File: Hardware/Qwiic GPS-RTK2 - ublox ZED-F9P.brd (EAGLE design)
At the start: 43.2 x 43.2 mm, 136 parts, among them J1 Radio, J13 U.FL, J3 PTH, U2 3.3V, U3 ZED-F9P

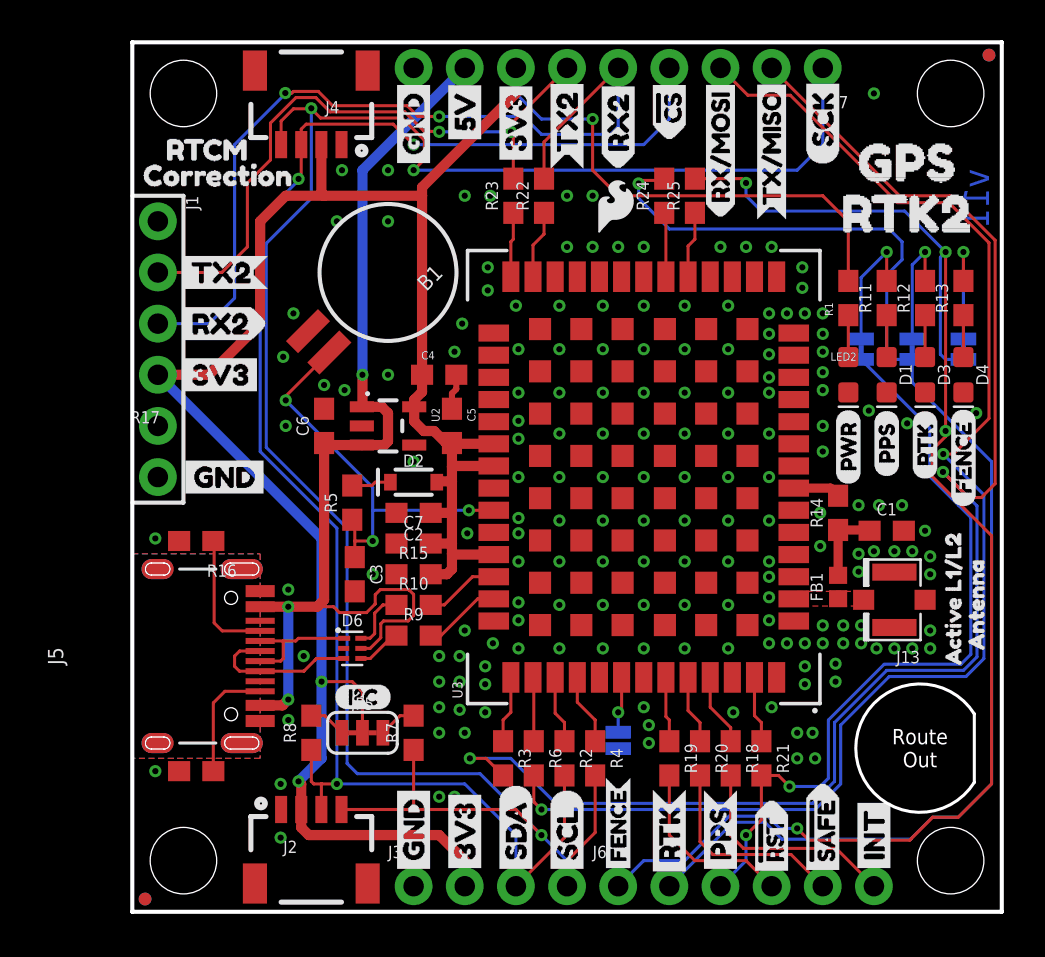
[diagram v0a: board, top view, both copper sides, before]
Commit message: Adding SMA connector to Antenna and SMA
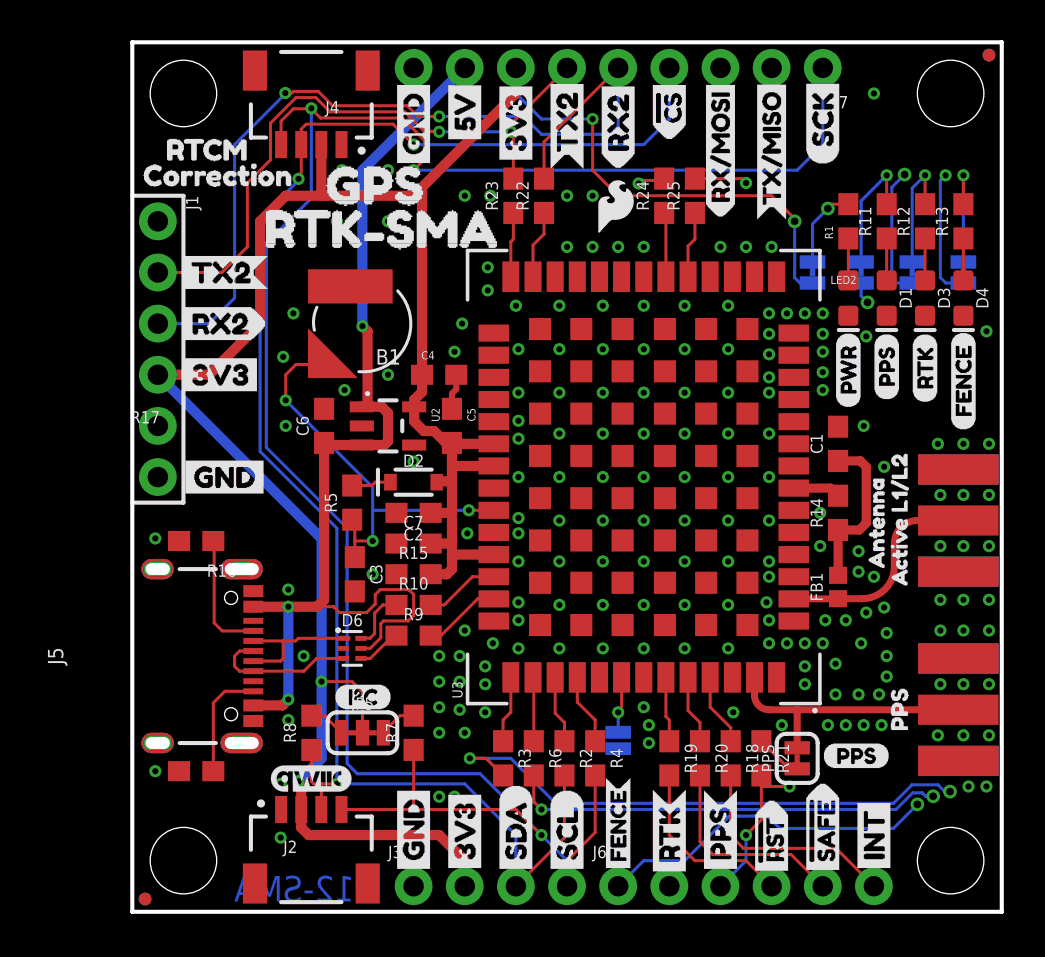
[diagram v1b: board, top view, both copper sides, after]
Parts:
- removed J13: U.FL, SparkFun-Connectors:U.FL
- removed JP1, JP2, JP3: (no value), SparkFun-Jumpers:SMT-JUMPER_2_NC_TRACE_SILK
- removed U$46: (no value), buzzard_labels (4):GPS#RTK28
- removed U$64: (no value), buzzard_labels (4):RTK21
- added E1, E2: SMA, SparkFun-RF:SMA-EDGE
- added FENCE, PPS, PPS_LED, PWR, RTK: (no value), SparkFun-Jumpers:SMT-JUMPER_2_NC_TRACE_SILK
- added U$47, U$74: (no value), buzzard_labels (2):PPS1
- added U$72: (no value), buzzard_labels (33):PPS0
- added U$73: (no value), buzzard_labels (3):RTK#SMA4
- added U$75: (no value), buzzard_labels (8):ANTENNA2
- added U$76: (no value), buzzard_labels (4):GPS#RTK#SMA5
- B1: device SparkFun-Batteries:BATTCON-6.8MM -> SparkFun-Batteries:ML414H_IV01E
- FB1: value FERRITE_BEAD-120_OHM-0402 -> 120_OHM
- J2, J4: value (none) -> Qwiic Right Angle; device SparkFun-Connectors:1X04_1MM_RA -> SparkFun-Connectors:JST04_1MM_RA
- J5: device SparkFun-Connectors:USB-C-16P -> SparkFun-Connectors:USB-C-16P-2LAYER-PADS
- U$12: device buzzard_labels:JP20 -> Labels:PWR-()-03
- U$25: device buzzard_labels (5):JP10 -> buzzard_labels (33):PPS0
- U$30: device Labels:QWIIC-LOGO-MEDIUM -> SparkFun-Aesthetics:QWIIC_4MM
- U$32: device buzzard_labels (5):JP32 -> buzzard_labels:RTK1
- U$54: value SMA-ANTENNA-THREADED -> (none); device SparkFun-Hardware:SMA-THREADED -> buzzard_labels:FENCE2
- moved U$59 26.4 mm to (8.00, 36.1)
- moved U$54 25.1 mm to (41.3, 33.1), flipped to the bottom, turned to 90 degrees
- moved U$71 6.41 mm to (37.0, 16.4)
- moved U$12 6.17 mm to (33.8, 33.1)
- moved C1 4.95 mm to (35.1, 23.2), turned to 90 degrees
- moved U$65 4.76 mm to (38.1, 15.5)
- moved U$32 4.47 mm to (38.7, 33.1)
- moved U$11 3.81 mm to (41.3, 23.9)
- moved D1 3.81 mm to (37.5, 30.5)
- moved D3 3.81 mm to (39.4, 30.5)
- moved D4 3.81 mm to (41.3, 30.5)
- moved LED2 3.81 mm to (35.6, 30.5)
- moved R1 3.81 mm to (35.6, 34.3)
- moved R11 3.81 mm to (37.5, 34.3)
- moved R12 3.81 mm to (39.4, 34.3)
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- renumbered JP4 to SPI
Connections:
- removed net SHLD: J5.SHLD1, J5.SHLD2, J5.SHLD3, J5.SHLD4, J5.SHLD5, J5.SHLD6, J5.SHLD7, J5.SHLD8
- new net N$21: PPS.1, R21.1
- new net PPS_STAT: J6.3, PPS_LED.2, R21.2
- net 3.3V: now also PWR.2; no longer R1.2
- net FENCE_STAT: now also FENCE.2; no longer JP3.2
- net GND: now also E1.GND@0, E1.GND@1, E1.GND@2, E1.GND@3, E2.GND@0, E2.GND@1, E2.GND@2, E2.GND@3, J5.SHLD1, J5.SHLD2, J5.SHLD3, J5.SHLD4; no longer J13.1, J13.2
- net GPS_ANT1: now also E1.SIG; no longer J13.FEED
- net N$17: now also PWR.1, R1.2; no longer R21.1, U3.53
- net N$3: now also RTK.1; no longer JP2.1
- net N$4: now also PPS_LED.1; no longer JP1.1
- net N$9: now also FENCE.1; no longer JP3.1
- net PPS: now also E2.SIG, PPS.2, U3.53; no longer J6.3, JP1.2, R21.2
- net RTK_STAT: now also RTK.2; no longer JP2.2
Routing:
- net PPS_STAT: track 0.00 -> 38.2 mm, vias 0 -> 3
- net PPS: track 38.3 -> 13.2 mm, vias 2 -> 0
- net GPS_ANT1: track 0.00 -> 10.5 mm
- net ANT_VCC: track 3.83 -> 8.10 mm
- net N$21: track 0.00 -> 2.35 mm
- net RTK_STAT: track 64.9 -> 66.9 mm, vias 1 -> 2
- net 3.3V: track 126.5 -> 124.8 mm, vias 3 -> 4
- net RXI/MOSI: track 68.3 -> 69.9 mm
- net TXO/MISO: track 72.9 -> 74.1 mm
- net FENCE_STAT: track 70.3 -> 69.2 mm, vias 4 -> 3
- net 5V: track 52.8 -> 53.6 mm
- net N$17: track 3.31 -> 4.07 mm, vias 0 -> 1
- net UNP_D-: track 6.29 -> 6.97 mm
- net GND: vias 174 -> 185
- added copper zone on layer 15, net GND
- added copper zone on layer 2, net GND
- removed copper zone on layer 1, net GPS_ANT1
- removed copper zone on layer 1, net SHLD
- removed copper zone on layer 16, net SHLD
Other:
- board text added: "4 Layer Board"
- board text added: "Board thickness is 1.6mm"
- board text added: "v12-SMA"
- board text removed: "Board thickness is 0.8mm"
- board text removed: "v11"
